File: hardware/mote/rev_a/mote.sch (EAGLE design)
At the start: 13 parts, among them U1 NRF52840

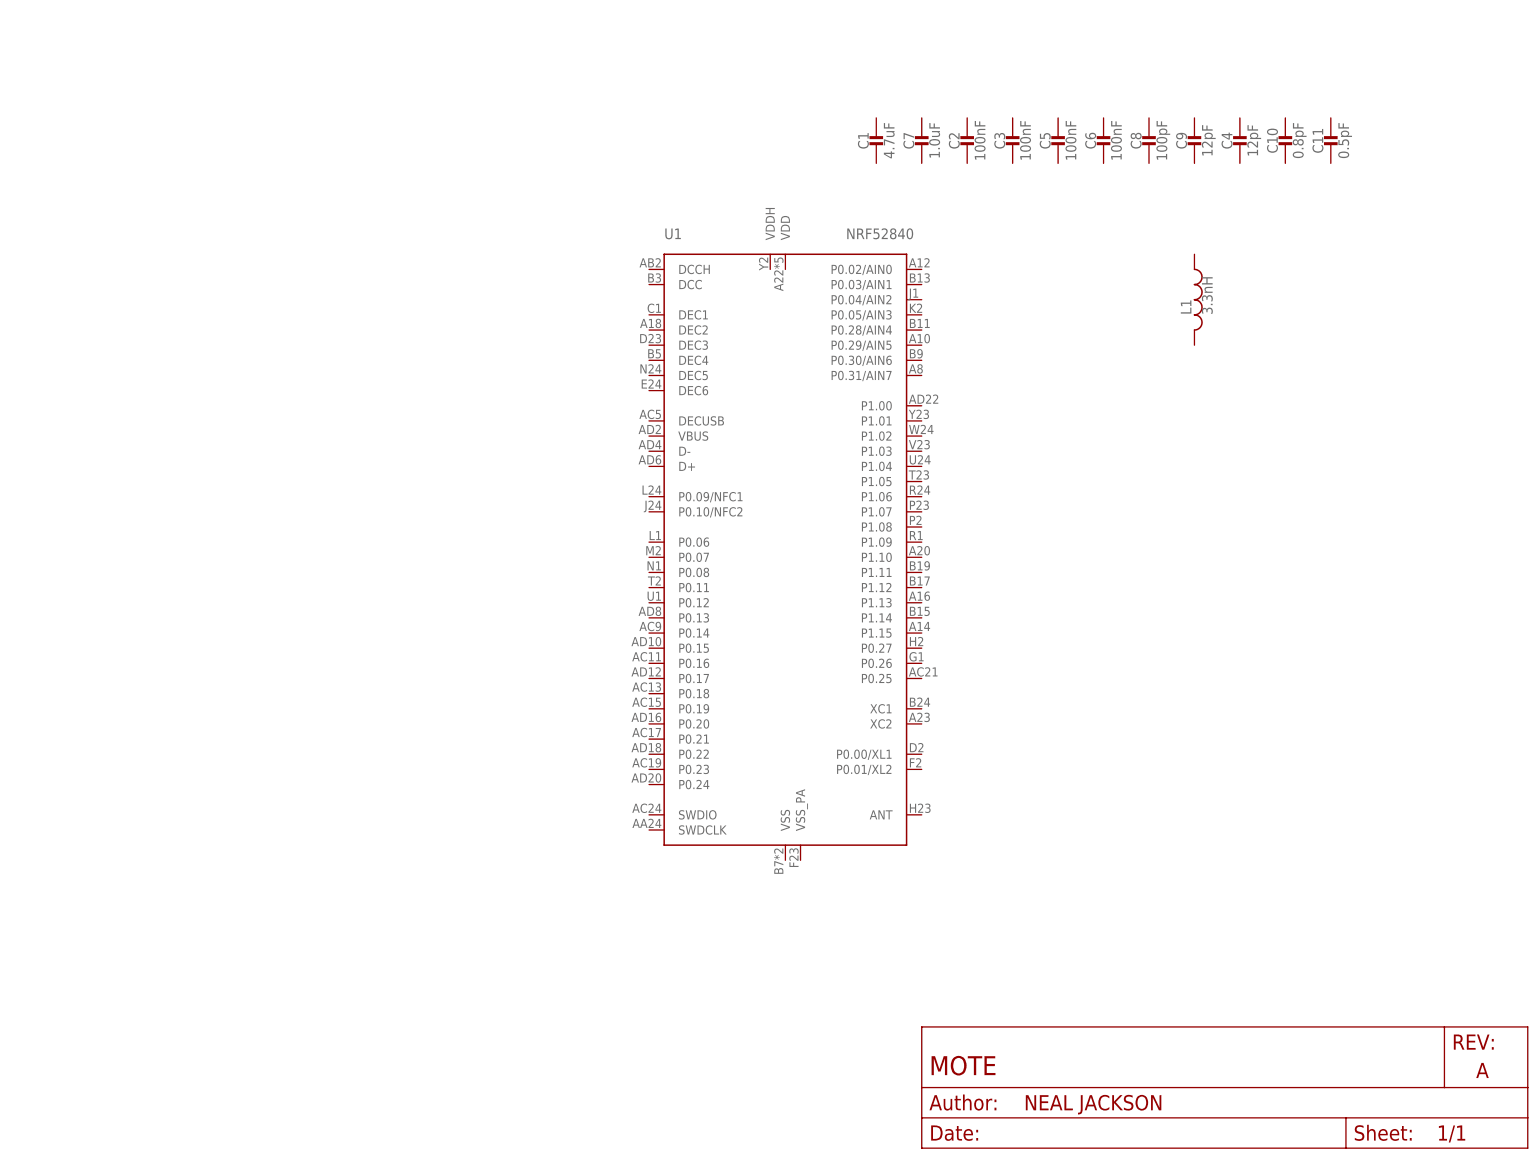
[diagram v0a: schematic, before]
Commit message: NRF + passives schematic done
Placement on board and preliminary routing
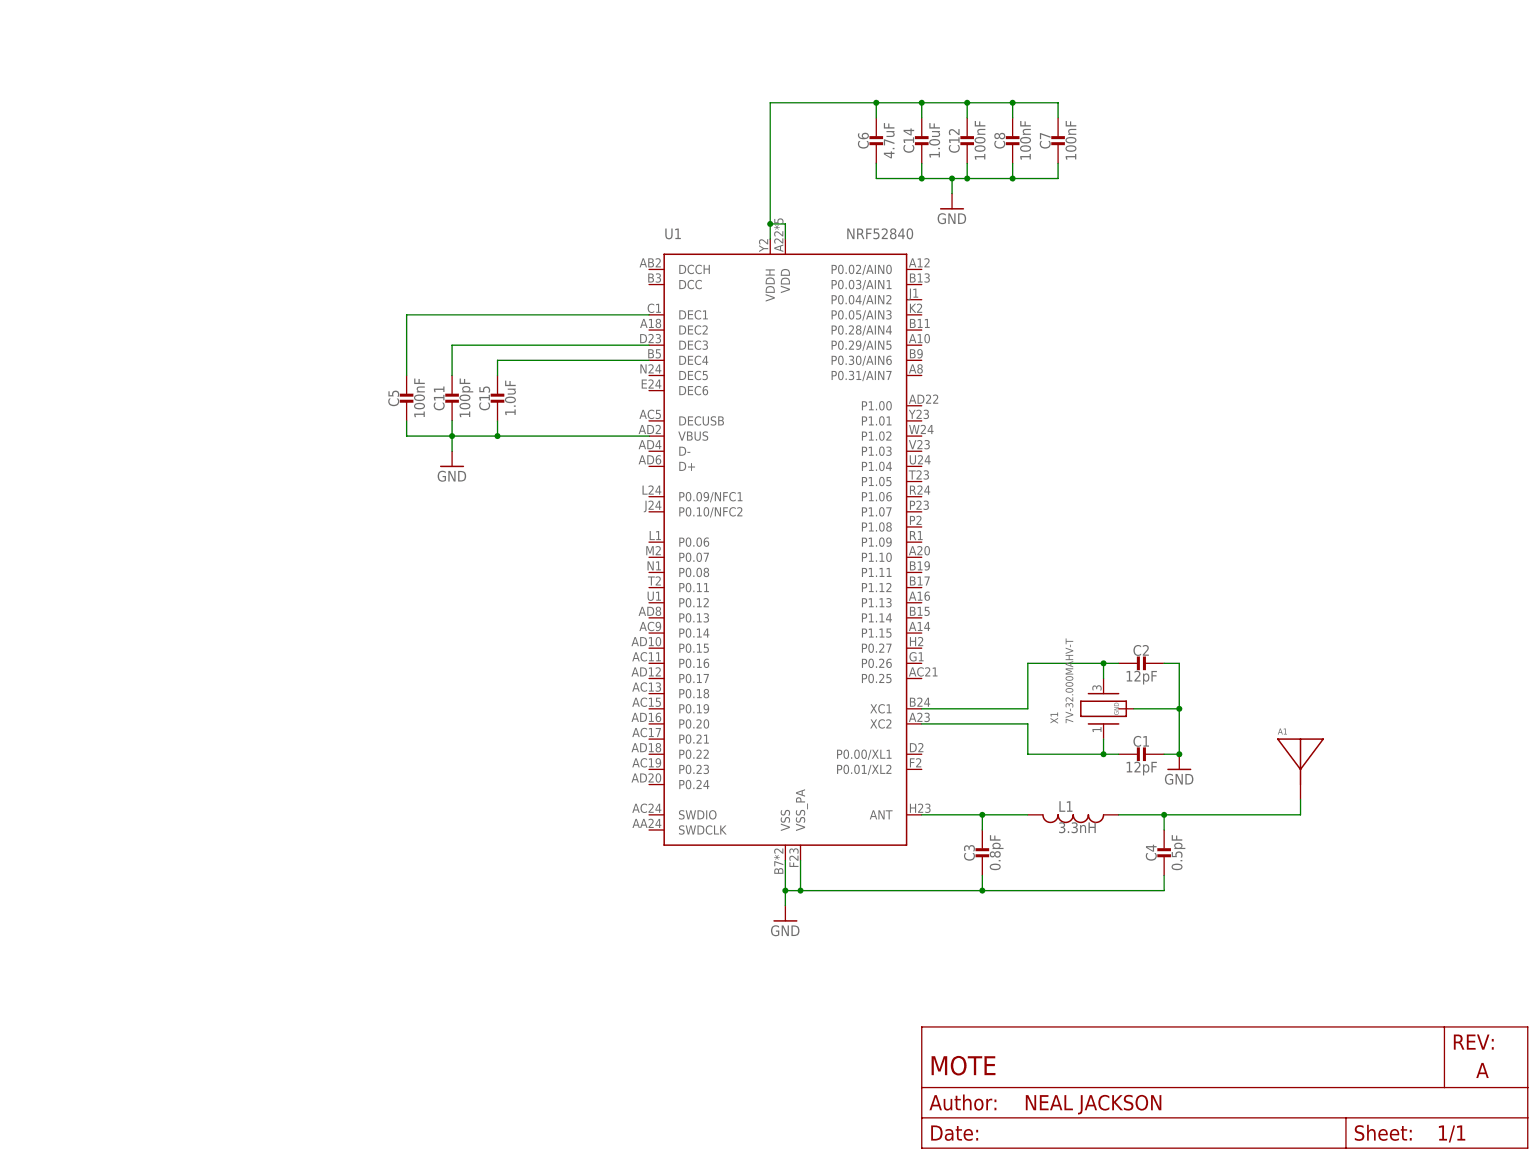
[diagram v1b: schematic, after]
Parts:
- removed C10: 0.8pF, passives:CAPACITOR0402_CAP
- removed C9: 12pF, passives:CAPACITOR0402_CAP
- added A1: (no value), chips:AH212M
- added C12: 100nF, passives:CAPACITOR0402_CAP
- added C14, C15: 1.0uF, passives:CAPACITOR0402_CAP
- added X1: 7V-32.000MAHV-T, crystals:7V-32.000MAHV-T
- C1: value 4.7uF -> 12pF; device passives:CAPACITOR0603_CAP -> passives:CAPACITOR0402_CAP; DIGIKEY 1276-2087-1-ND -> 490-6197-1-ND
- C11: value 0.5pF -> 100pF; DIGIKEY 490-6264-1-ND -> 490-5922-1-ND
- C2: value 100nF -> 12pF; DIGIKEY 490-6328-1-ND -> 490-6197-1-ND
- C3: value 100nF -> 0.8pF; DIGIKEY 490-6328-1-ND -> 490-11253-1-ND
- C4: value 12pF -> 0.5pF; DIGIKEY 490-6197-1-ND -> 490-6264-1-ND
- C6: value 100nF -> 4.7uF; device passives:CAPACITOR0402_CAP -> passives:CAPACITOR0603_CAP; DIGIKEY 490-6328-1-ND -> 1276-2087-1-ND
- C7: value 1.0uF -> 100nF; device passives:CAPACITOR0603_CAP -> passives:CAPACITOR0402_CAP; DIGIKEY 490-7195-1-ND -> 490-6328-1-ND
- C8: value 100pF -> 100nF; DIGIKEY 490-5922-1-ND -> 490-6328-1-ND
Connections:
- new net GND: C1.1, C11.2, C12.2, C14.2, C15.2, C2.1, C3.2, C4.2, C5.2, C6.2, C7.2, C8.2, U1.VBUS, U1.VSS, U1.VSS_PA, X1.GND
- new net N$1: C12.1, C14.1, C6.1, C7.1, C8.1, U1.VDD, U1.VDDH
- new net N$2: C5.1, U1.DEC1
- new net N$3: C15.1, U1.DEC4
- new net N$4: C11.1, U1.DEC3
- new net N$5: C3.1, L1.2, U1.ANT
- new net N$6: A1.ANTENNA, C4.1, L1.1
- new net N$8: C2.2, U1.XC1, X1.2
- new net N$9: C1.2, U1.XC2, X1.1
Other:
- moved on the sheet: C1, C11, C2, C3, C4, C5, C6, C7, C8, L1, U1

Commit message: front end overvolt
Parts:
- added BAT1: LTOHTC1020, batteries:LTOHTC1020
- added C13, C16: 10uF, passives:CAPACITOR0603_CAP
- added D1: SOLARCELL, mote:SOLARCELL
- added L3: 1uH, passives:INDUCTORIHL2525CZ
- added Q1: CSD22206W, fets:CSD22206W
- added R1: 1k, passives:RESISTOR0402_RES
- added R2: 80.6k, passives:RESISTOR0603_RES
- added R3: 20, passives:RESISTOR0402_RES
- added R4: 33M, passives:RESISTOR0603_RES
- added U2: (no value), chips:ADM8641
- added U3: MAX17222, chips:MAX17222
- added U4: TPS3839G25DBZ, chips:TPS3839G25DBZ
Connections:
- new net ENABLE: R4.2
- new net N$10: BAT1.-, D1.V-, R3.1, U2.GND
- new net N$11: Q1.G, R1.1, U2.OUT
- new net N$12: R2.2, U3.SEL
- new net N$13: Q1.S, R3.2, U4.GND
- new net N$14: R4.1, U3.EN
- new net SW1: L3.2, U3.LX
- new net VBAT: C13.1, L3.1, U3.IN
- new net VCC: C12.1, C14.1, C16.1, C6.1, C7.1, C8.1, U1.VDD, U1.VDDH, U3.OUT
- net GND: now also C13.2, C16.2, R2.1, U3.GND
- net N$1: now also BAT1.+, D1.V+, Q1.D, R1.2, U2.!DIS, U2.VCC, U4.VDD; no longer C12.1, C14.1, C6.1, C7.1, C8.1, U1.VDD, U1.VDDH
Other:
- note added: "NRF52840"
- note added: "Over voltage discharge path"

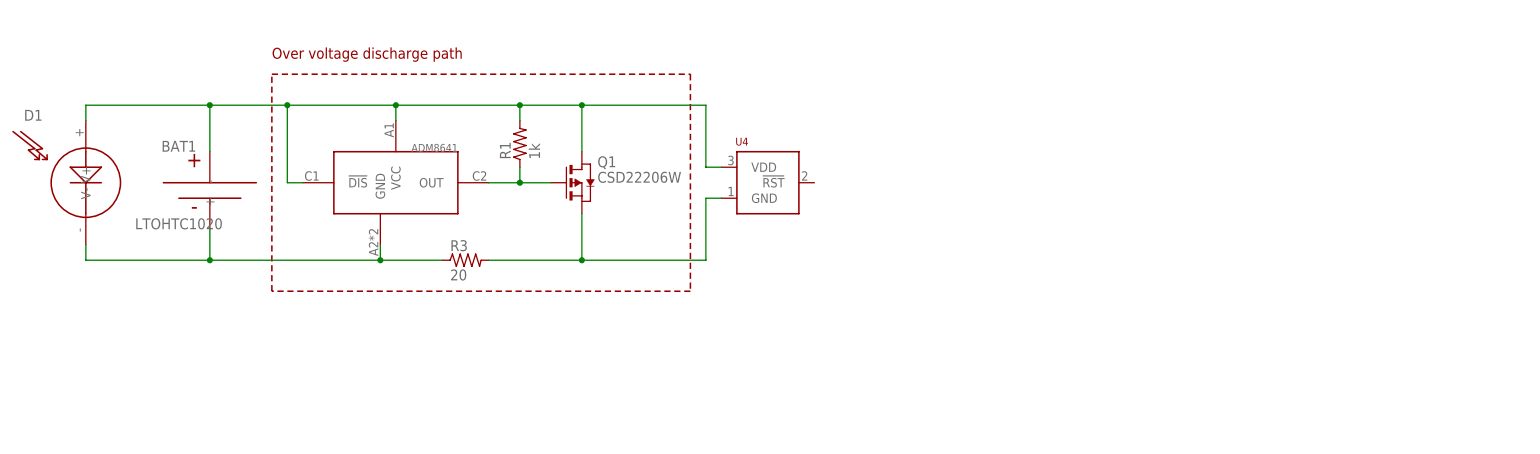
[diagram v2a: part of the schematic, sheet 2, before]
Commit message: Add start of source switching
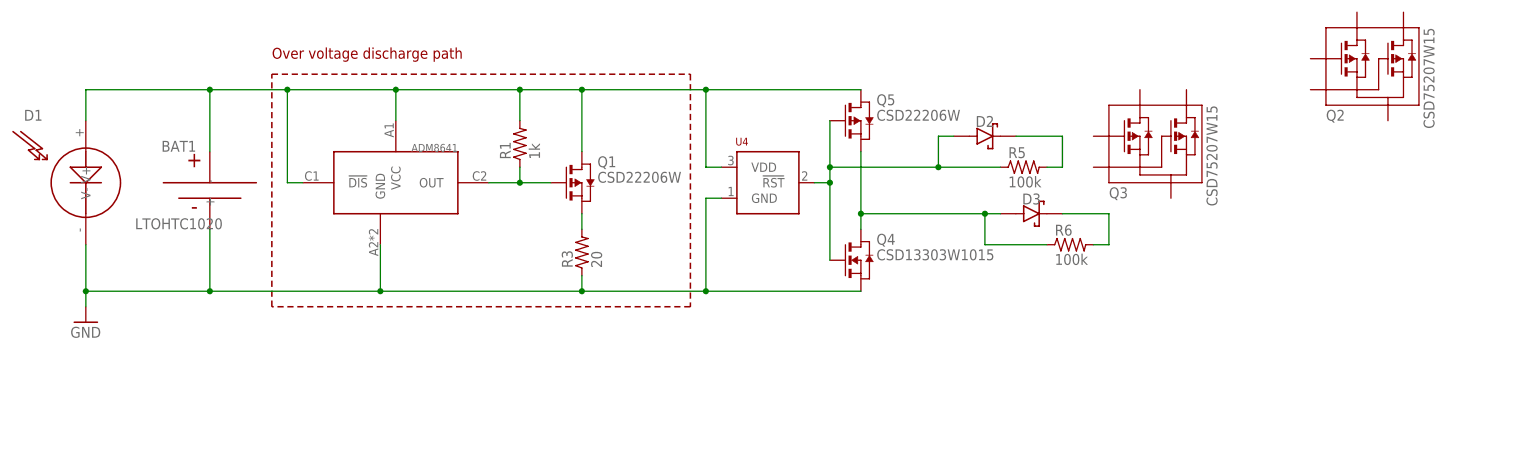
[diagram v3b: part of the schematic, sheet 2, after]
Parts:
- added D2, D3: DIODE_SCHOTTKYSOD323, passives:DIODE_SCHOTTKYSOD323
- added Q2, Q3: CSD75207W15, fets:CSD75207W15
- added Q4: CSD13303W1015, fets:CSD13303W1015
- added Q5: CSD22206W, fets:CSD22206W
- added R5, R6: 100k, passives:RESISTOR0402_RES
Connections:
- new net N$15: D3.ANODE, Q4.D, Q5.S, R6.1
- new net N$16: D3.CATHODE, R6.2
- new net N$17: Q1.S, R3.2
- net GND: now also BAT1.-, D1.V-, Q4.S, R3.1, U2.GND, U4.GND
- net N$1: now also Q5.D
- net N$10: now also D2.ANODE, Q4.G, Q5.G, R5.1, U4.!RST; no longer BAT1.-, D1.V-, R3.1, U2.GND
- net N$13: now also D2.CATHODE, R5.2; no longer Q1.S, R3.2, U4.GND
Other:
- moved on the sheet: R3

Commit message: finish power supply, rtc
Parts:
- added BT1: BAT_PACK2/3AA, batteries:BAT_PACK2/3AA
- added BT2: BAT_PACKAA, batteries:BAT_PACKAA
- added BT3: BAT_PACKCR123A, batteries:BAT_PACKCR123A
- added C10: 1uF, passives:CAPACITOR0402_CAP
- added C17, C18: DNP, passives:CAPACITOR0402_CAP
- added C9: 47pF, passives:CAPACITOR0402_CAP
- added TP1, TP10, TP11, TP2, TP3, TP4, TP5, TP6, TP7, TP8, TP9: TEST_POINT_0.040IN, headers:TEST_POINT_0.040IN
- added U5: AB1815-T3, chips:AB1815-T3
- added X2: ABS07-32.768KHZ-7-T, crystals:ABS07-32.768KHZ-7-T
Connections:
- new net !RTC_EXTR: U5.!EXTR
- new net !RTC_IRQ1: U5.FOUT/!IRQ1
- new net !RTC_IRQ2: U5.!IRQ2
- new net !RTC_RESET: U5.!RST
- new net CLKOUT: U1.P0.00/XL1, U5.CLKOUT/!IRQ3
- new net CS_RTC: U5.!CS
- new net MISO: U5.SDO
- new net MOSI: U5.SDI
- new net N$18: D3.CATHODE, Q3.G1, Q3.G2, R6.2, TP6.TESTPOINT
- new net N$19: C17.1, U5.XI, X2.1
- new net N$20: C18.1, U5.XO, X2.2
- new net N$21: C9.1, U5.AF
- new net N$22: BT1.+, BT2.+, BT3.+, Q3.D1, TP9.TESTPOINT
- new net N$24: BAT1.+, D1.V+, Q1.D, Q2.D1, Q5.D, R1.2, TP1.TESTPOINT, U2.!DIS, U2.VCC, U4.VDD
- new net SCL: U5.SCL
- new net WDI: U5.WDI
- net GND: now also BT1.-, BT2.-, BT3.-, C10.2, C17.2, C18.2, C9.2, U1.P0.01/XL2, U5.VSS
- net N$1: now also D2.ANODE, Q4.D, Q5.S, R5.1, TP4.TESTPOINT; no longer BAT1.+, D1.V+, Q1.D, Q5.D, R1.2, U2.!DIS, U2.VCC, U4.VDD
- net N$10: now also Q2.S, TP7.TESTPOINT; no longer D2.ANODE, Q4.G, Q5.G, R5.1, U4.!RST
- net N$11: now also TP2.TESTPOINT
- net N$13: now also Q2.G1, Q2.G2, TP5.TESTPOINT
- net N$15: now also Q4.G, Q5.G, TP3.TESTPOINT, U4.!RST; no longer Q4.D, Q5.S
- net N$16: now also Q3.S, TP8.TESTPOINT; no longer D3.CATHODE, R6.2
- net SW1: now also TP11.TESTPOINT
- net VBAT: now also Q2.D2, Q3.D2, TP10.TESTPOINT
- net VCC: now also C10.1, U5.VCC
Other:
- note added: "Note: Only populate one type of battery holder"
- note added: "Power Supply"
- note added: "Under voltage supply switch"
